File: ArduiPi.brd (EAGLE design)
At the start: 85 x 56 mm, 97 parts, among them IC1 AVR-MEGA8-PPTH, IC2 DS2482-100S, J1 Teleinfo, J11 DNP, J12 DNP, J13 DNP, J2 DNP, J3 DNP, J4 DNP, J5 DNP, J6 DNP, J7 DNP, J8 DNP, J9 DC-044-AH, Q1 BSS138, Q2 BSS138, Q3 BSS138, Q4 BSS138, Q5 BSS84, U1 78M05, U2 LD1117 3V3, U3 TXB0104, U4 TXB0108, U5 TXB0108, X1 16Mhz

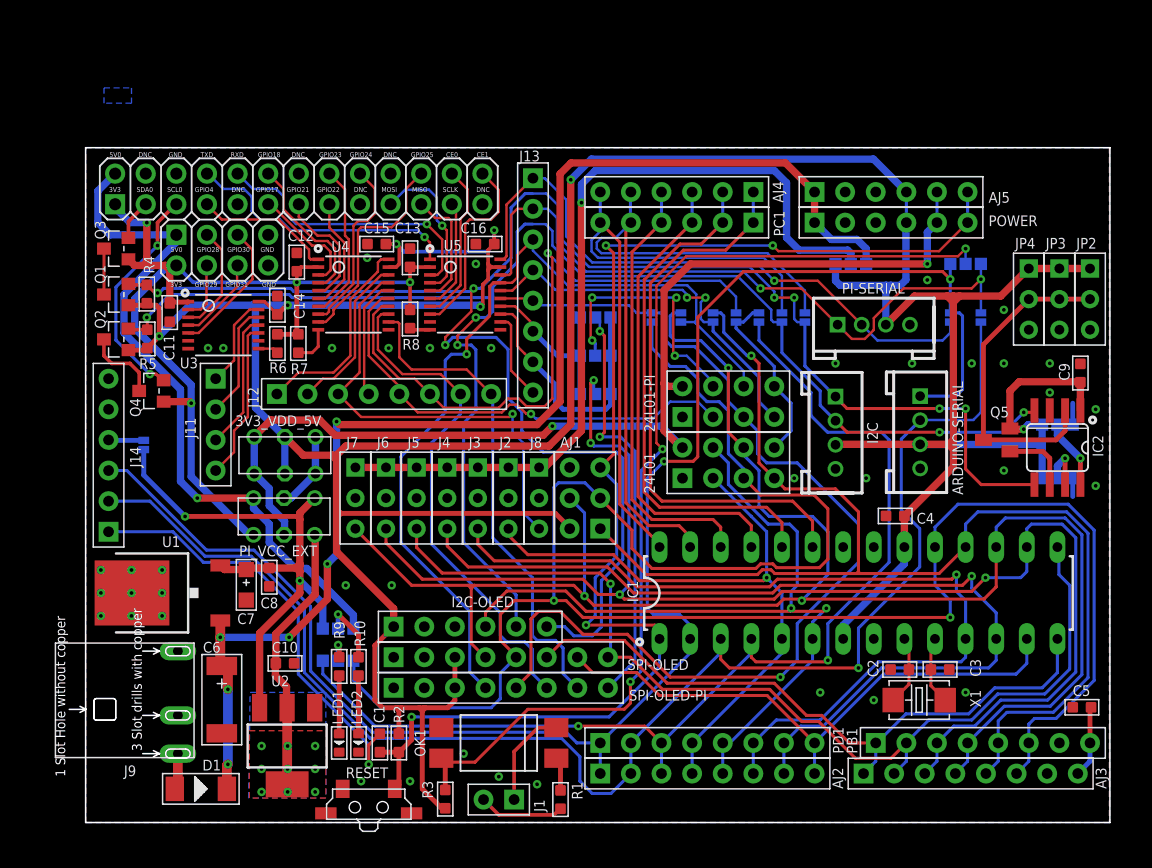
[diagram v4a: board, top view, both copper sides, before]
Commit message: 2nd Prototype Board
2nd Version of the prototype board, near final version.

Changes :

- Removed R3 pullup from the output of the SFH6206
- Changed Level Shifting of RX line, now goes through 2 new FET
transistors Q7 and Q6 (BSS138 like I2C) and removed the connection of RX
from the TXB0108 (U5)
- Letting 2 TXB0108 of U5 ports free, I decided to bring them to
end users (if they need) putting 2 soldering pad JFREE1 and JFREE2 and
removed the pull down R12
- Changed soldering pad connection of TX/RX from Arduino to PI by
jumper because is we connect Arduino with Pi by serial, this will
conflict
during Arduino programming using FTDI cable. With jumpers we could
remove them during the firmware upload on the Arduino and put them back
after (much easier than solder/unsolder)
- Added a test led on PI I/O, because when I test program on PI I
do not have any indicator the program is working fine, so this led could
be
setup to blink in the program as visual test
- Added a new soldering pad to choose who drive the RST Line of I2C
OLED connector (I/O port of Pi or Arduino) letting user to choose what
will
drive this OLED by I2C (Pi or Arduino)
- Changed R10 and R11 value to 1K and R9 value to 470
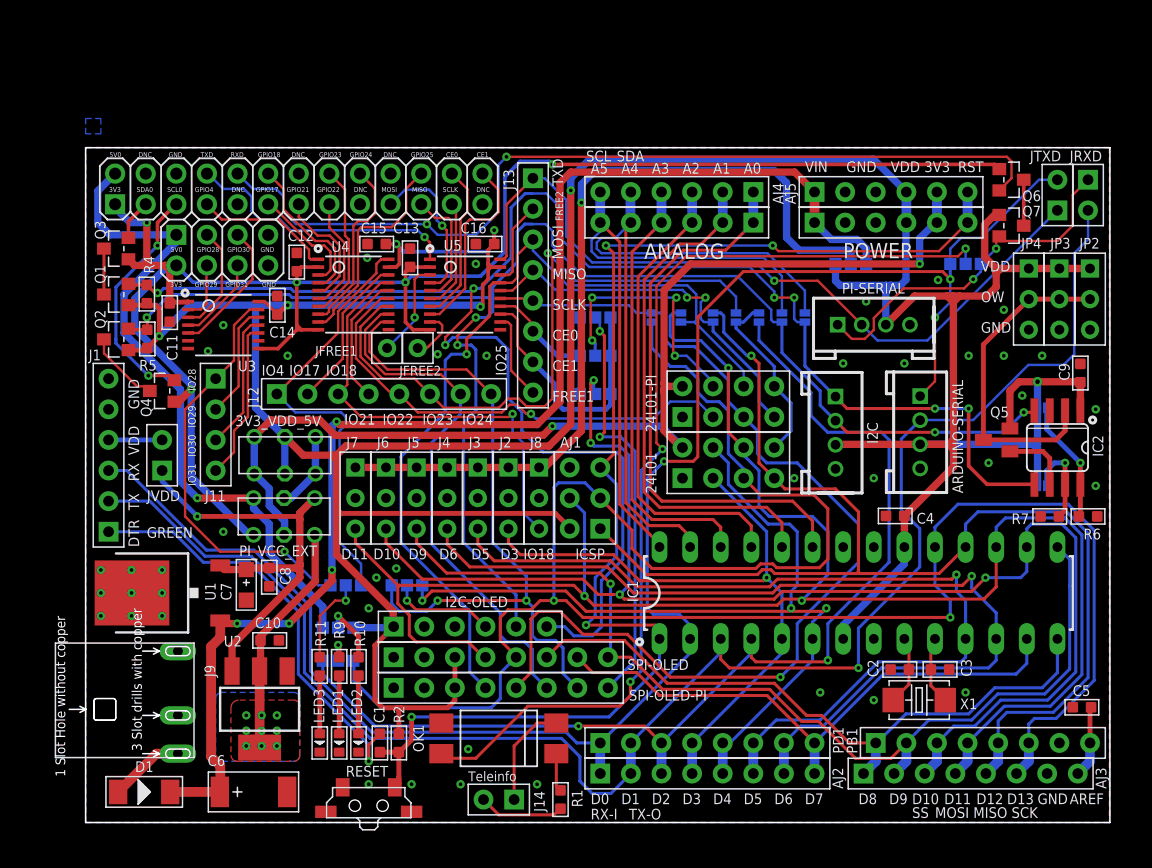
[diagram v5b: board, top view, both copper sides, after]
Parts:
- removed PRX: PRX, Discrete:2P-SMD-1.78X1.27
- removed PTX: PTX, Discrete:2P-SMD-1.78X1.27
- removed PVDD: PVDD, Discrete:2P-SMD-1.78X1.27
- removed R3: 4.7k, Discrete:R0603
- removed R8: 10k, Discrete:R0603
- added JFREE1, JFREE2: (no value), Seeedstudio-Connector:1P-60/32MIL
- added JRXD: J2, Seeedstudio-Connector:2P-2.54
- added JTXD: J1, Seeedstudio-Connector:2P-2.54
- added JVDD: FTDI Powered, Seeedstudio-Connector:2P-2.54
- added LED3: RED, Discrete:LED-0603
- added PI2C, PLED3: (no value), Discrete:3P-SMD-4.1X1.5
- added Q6, Q7: BSS138, Seeedstudio-Discreter.rpt:SOT23
- added R11: 1k, Discrete:R0603
- J1: value Teleinfo -> (none); device Seeedstudio-Connector:2P-2.54 -> Connector:6P-2.54-65/35MIL
- J14: value (none) -> Teleinfo; device Connector:6P-2.54-65/35MIL -> Seeedstudio-Connector:2P-2.54
- LED2: value RED -> GREEN
- PAD1: value (none) -> PAD1; device Discrete:3P-SMD-4.1X1.5 -> Discrete:2P-SMD-1.78X1.27
- PAD2: value (none) -> PAD2; device Discrete:3P-SMD-4.1X1.5 -> Discrete:2P-SMD-1.78X1.27
- R1: value 1.2k -> 3.3k
- R10: value 600 -> 1k
- R9: value 360 -> 470
- moved R6 68.8 mm to (83.2, 25.4), turned to 180 degrees
- moved R7 64.0 mm to (80.0, 25.4), turned to 0 degrees
- moved J1 43.2 mm to (1.91, 30.5), turned to 180 degrees
- moved J14 43.2 mm to (34.3, 1.91), turned to 270 degrees
- moved C6 8.10 mm to (13.9, 2.54), turned to 0 degrees
- moved D1 4.71 mm to (4.86, 2.54)
- moved U2 3.81 mm to (14.4, 9.40)
- moved U$6 2.69 mm to (32.5, 45.0)
- moved U$3 2.54 mm to (29.8, 41.5)
- moved C10 2.29 mm to (15.3, 15.1)
- moved PAD2 1.89 mm to (79.4, 34.4), turned to 90 degrees
- moved PAD1 1.42 mm to (79.4, 27.9), turned to 90 degrees
- moved Q4 0.89 mm to (6.35, 35.8)
- moved OK1 0.38 mm to (34.3, 6.99)
- moved RESET 0.13 mm to (23.5, 1.40)
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- renumbered PC1 to ANALOG
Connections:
- net CE3 renamed FREE1
- new net FREE1-PI: JFREE1.P$1, U5.3
- new net FREE2: J13.2, U5.18
- new net FREE2-PI: JFREE2.P$1, U5.9
- new net OLED-RST: I2C-OLED.4, PI2C.MM
- net 3V3-PI: now also Q6.1, U3.8, U4.10, U5.10; no longer R6.2, R7.2, R8.2
- net 5V-EXT: now also JVDD.1; no longer PLED2.00, PVDD.2
- net D0/RX-I: now also J1.3, JTXD.2; no longer J14.3, PRX.2
- net D1/TX-O: now also J1.2, JRXD.2; no longer J14.2, PTX.2
- net D4: now also PI2C.11; no longer I2C-OLED.4
- net DTR: now also J1.1; no longer J14.1
- net GND: now also J1.5, J1.6, LED3.-, R6.1, R7.1; no longer J14.5, J14.6, PAD1.00, PAD2.00
- net IO25: now also PI2C.00
- net IO28: now also PLED3.00
- net IO4: now also PLED3.11
- net N$1: no longer R3.1
- net N$10: now also J1.4, JVDD.2; no longer J14.4, PVDD.1
- net N$11: now also PAD1.1, R7.2; no longer PAD1.MM
- net N$13: now also LED3.+, R11.2; no longer R8.1, U5.10
- net N$14: now also J14.2; no longer J1.2
- net N$19: now also PLED3.MM, R11.1; no longer R6.1, U3.8
- net N$2: now also PAD2.1, R6.2; no longer PAD2.MM
- net N$7: now also Q6.3, Q7.3; no longer R7.1, U4.10
- net N$9: now also J14.1; no longer J1.1
- net RXD: now also JRXD.1, Q7.2; no longer J13.2, PTX.1, U5.18
- net RXD-PI: now also Q6.2; no longer U5.3
- net TXD: now also JTXD.1; no longer PRX.1
- net VDD: now also PAD1.2, PAD2.2, PLED2.00, Q7.1; no longer PAD1.11, PAD2.11, R3.2
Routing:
- net 3V3-PI: track 82.8 -> 146.7 mm, vias 4 -> 5
- net RXD-PI: track 23.7 -> 75.1 mm, vias 1 -> 2
- net RXD: track 57.3 -> 30.0 mm
- net IO28: track 7.64 -> 34.6 mm, vias 0 -> 1
- net IO4: track 17.1 -> 36.8 mm
- net IO25: track 40.9 -> 56.6 mm, vias 0 -> 2
- net D1/TX-O: track 122.8 -> 137.4 mm
- net TXD: track 51.1 -> 63.4 mm
- net 5V-EXT: track 48.6 -> 38.8 mm, vias 2 -> 1
- net D0/RX-I: track 138.0 -> 147.5 mm, vias 2 -> 3
- net OLED-RST: track 0.00 -> 8.68 mm, vias 0 -> 1
- net FREE1-PI: track 0.00 -> 8.08 mm, vias 0 -> 1
- net FREE2: track 0.00 -> 7.04 mm
- net N$19: track 1.70 -> 7.38 mm, vias 0 -> 1
- net D11/MOSI: track 145.8 -> 151.3 mm
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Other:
- board text added: "3V3"
- board text added: "5V-PI"
- board text added: "A0"
- board text added: "A1"
- board text added: "A2"
- board text added: "A3"
- board text added: "A4"
- board text added: "A5"
- board text added: "AREF"
- board text added: "Arduino"
- board text added: "CE0"
- board text added: "CE1"
- board text added: "D0"
- board text added: "D1"
- board text added: "D10"
- board text added: "D11"
- board text added: "D12"
- board text added: "D13"
- board text added: "D2"
- board text added: "D3"
- board text added: "D4"
- board text added: "D5"
- board text added: "D6"
- board text added: "D7"
- board text added: "D8"
- board text added: "D9"
- board text added: "DTR"
- board text added: "Documentation at http://hallard.me"
- board text added: "FREE1"
- board text added: "FREE2"
- board text added: "GND"
- board text added: "GREEN"
- board text added: "ICSP"
- board text added: "IO17"
- board text added: "IO18"
- board text added: "IO21"
- board text added: "IO22"
- board text added: "IO23"
- board text added: "IO24"
- board text added: "IO25"
- board text added: "IO28"
- board text added: "IO29"
- board text added: "IO30"
- board text added: "IO31"
- board text added: "IO4"
- board text added: "MISO"
- board text added: "MOSI"
- board text added: "OW"
- board text added: "Pi"
- board text added: "RST"
- board text added: "RX"
- board text added: "RX-I"
- board text added: "SCK"
- board text added: "SCL"
- board text added: "SCLK"
- board text added: "SDA"
- board text added: "SS"
- board text added: "TX"
- board text added: "TX-O"
- board text added: "TXD"
- board text added: "Teleinfo"
- board text added: "VDD"
- board text added: "VIN"
- board text added: "v0.9c 03/04/2013"
- board text removed: "v0.9a 12/11/2012"

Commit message: ArduiPi Production Version V0.9d
ArduiPi Production Version V0.9d
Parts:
- moved U$6 3.09 mm to (35.6, 44.5)
- moved U$3 3.05 mm to (32.8, 40.6)
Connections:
- net GPIO28: now also PI-P1.P5.4; no longer PI-P1.P5.3
- net GPIO29: now also PI-P1.P5.3; no longer PI-P1.P5.4
- net GPIO30: now also PI-P1.P5.6; no longer PI-P1.P5.5
- net GPIO31: now also PI-P1.P5.5; no longer PI-P1.P5.6
- net SCL: now also I2C.1; no longer I2C.2
- net SDA: now also I2C.2; no longer I2C.1
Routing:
- net GPIO29: track 9.08 -> 5.40 mm
- net GPIO31: track 11.4 -> 7.74 mm
- net SDA: track 147.3 -> 150.7 mm, vias 7 -> 6
- net GPIO28: track 4.91 -> 8.04 mm
- net GPIO30: track 7.17 -> 9.64 mm
- net SCL: track 126.8 -> 126.1 mm
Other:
- board text added: "by Seeed Studio & Charles-Henri Hallard"
- board text added: "v0.9d 27/06/2013"
- board text removed: "by Seeed Studio"
- board text removed: "v0.9c 03/04/2013"
